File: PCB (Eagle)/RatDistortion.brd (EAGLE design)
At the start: 55 x 45 mm, 44 parts, among them IC1 LM308D

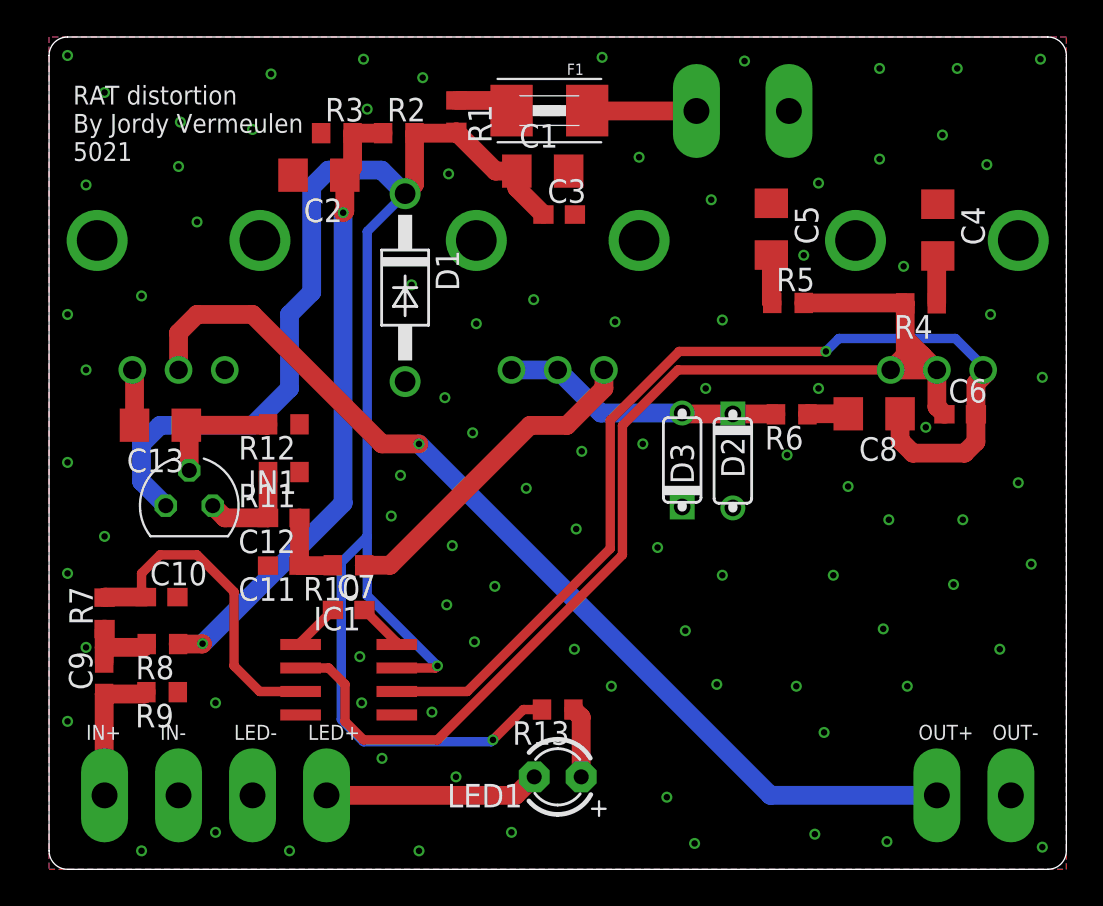
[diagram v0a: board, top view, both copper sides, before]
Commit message: Updated Eagle files
JFET 2N5458 (Q1 (was JN1)) in schematic is now correct icon (used default J201 device (same package and pinout)
Updated PCB to Q1 and made values more readable for documentation (Value will probably not be printed on Silk layer)
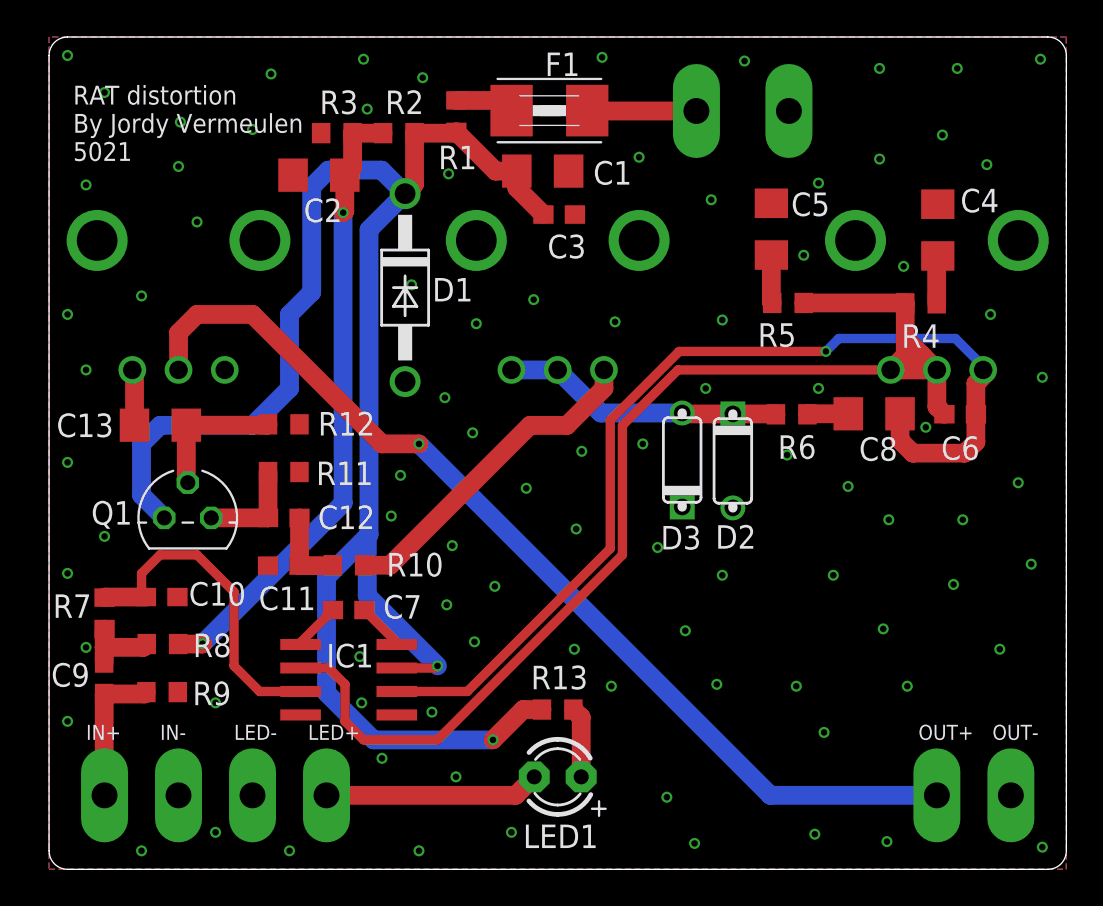
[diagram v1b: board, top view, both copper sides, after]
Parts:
- removed JN1: 2N5458, 2N5458:TO92
- added Q1: 2N5458, transistor-fet:TO92
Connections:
- removed net N$17: C13.1, JN1.2, R12.2
- new net N$11: C13.1, Q1.2, R12.2
- net 9V: now also Q1.3; no longer JN1.3
- net N$8: now also Q1.1; no longer JN1.1
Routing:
- net N$11: track 0.00 -> 7.58 mm
- net N$17: track 6.95 -> 0.00 mm
- net 9V: track 96.1 -> 96.9 mm

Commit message: Moved Q1 to own lib Eagle files
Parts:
- Q1: device transistor-fet:TO92 -> 2N5458_2:TO92
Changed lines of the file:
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@@
 <drawing>
 <settings>
-<setting alwaysvectorfont="yes"/>
+<setting alwaysvectorfont="no"/>
 <setting verticaltext="up"/>
 </settings>
@@
 <attribute name="VALUE" x="28.9075" y="39.115" size="0.6096" layer="27" rot="R180"/>
 </element>
-<element name="Q1" library="transistor-fet" library_urn="urn:adsk.eagle:library:396" package="TO92" package3d_urn="urn:adsk.eagle:package:28523/2" value="2N5458" x="7.5" y="19" smashed="yes">
+<element name="Q1" library="2N5458_2" package="TO92" package3d_urn="urn:adsk.eagle:package:28523/2" value="2N5458" x="7.5" y="19" smashed="yes">
 <attribute name="NAME" x="2.275" y="18.635" size="1.27" layer="25" ratio="10"/>
-<attribute name="POPULARITY" value="0" x="7.5" y="19" size="1.778" layer="27" display="off"/>
 <attribute name="VALUE" x="10.675" y="17.73" size="1.27" layer="27" ratio="10"/>
 </element>

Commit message: Update PCB
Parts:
- moved R10 1.26 mm to (16.1, 17.7)
- moved C7 1.00 mm to (16.2, 15.0)
- moved IC1 1.00 mm to (16.2, 11.2)
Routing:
- net N$12: track 18.0 -> 17.0 mm
- net 9V: track 96.9 -> 95.9 mm
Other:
- board text added: "+"
- board text added: "-"
- board text added: "RAT distortion 5021"
- board text removed: "RAT distortion By Jordy Vermeulen 5021"
- board text removed: "Signature"
